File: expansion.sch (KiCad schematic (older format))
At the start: 4 parts, among them J10 Conn_02x05_Odd_Even, J7 DF40HC(3.5)-60DS, J9 DF40HC(3.5)-60DS, U1 IMX8MM

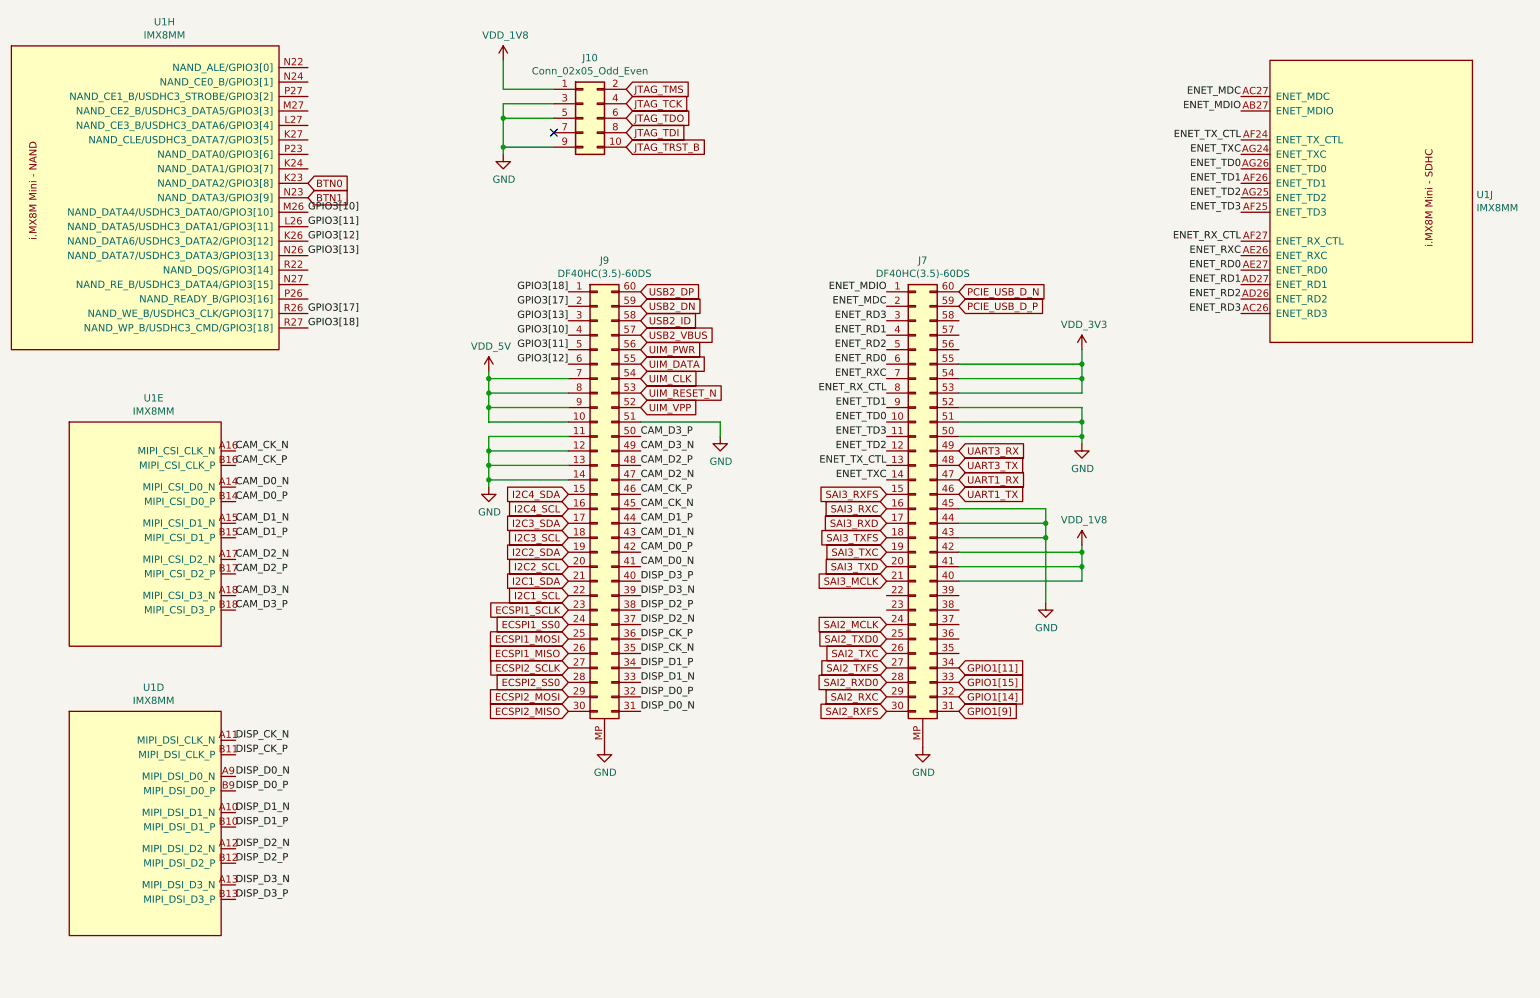
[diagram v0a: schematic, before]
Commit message: Change expansion audio routing to sai2/3
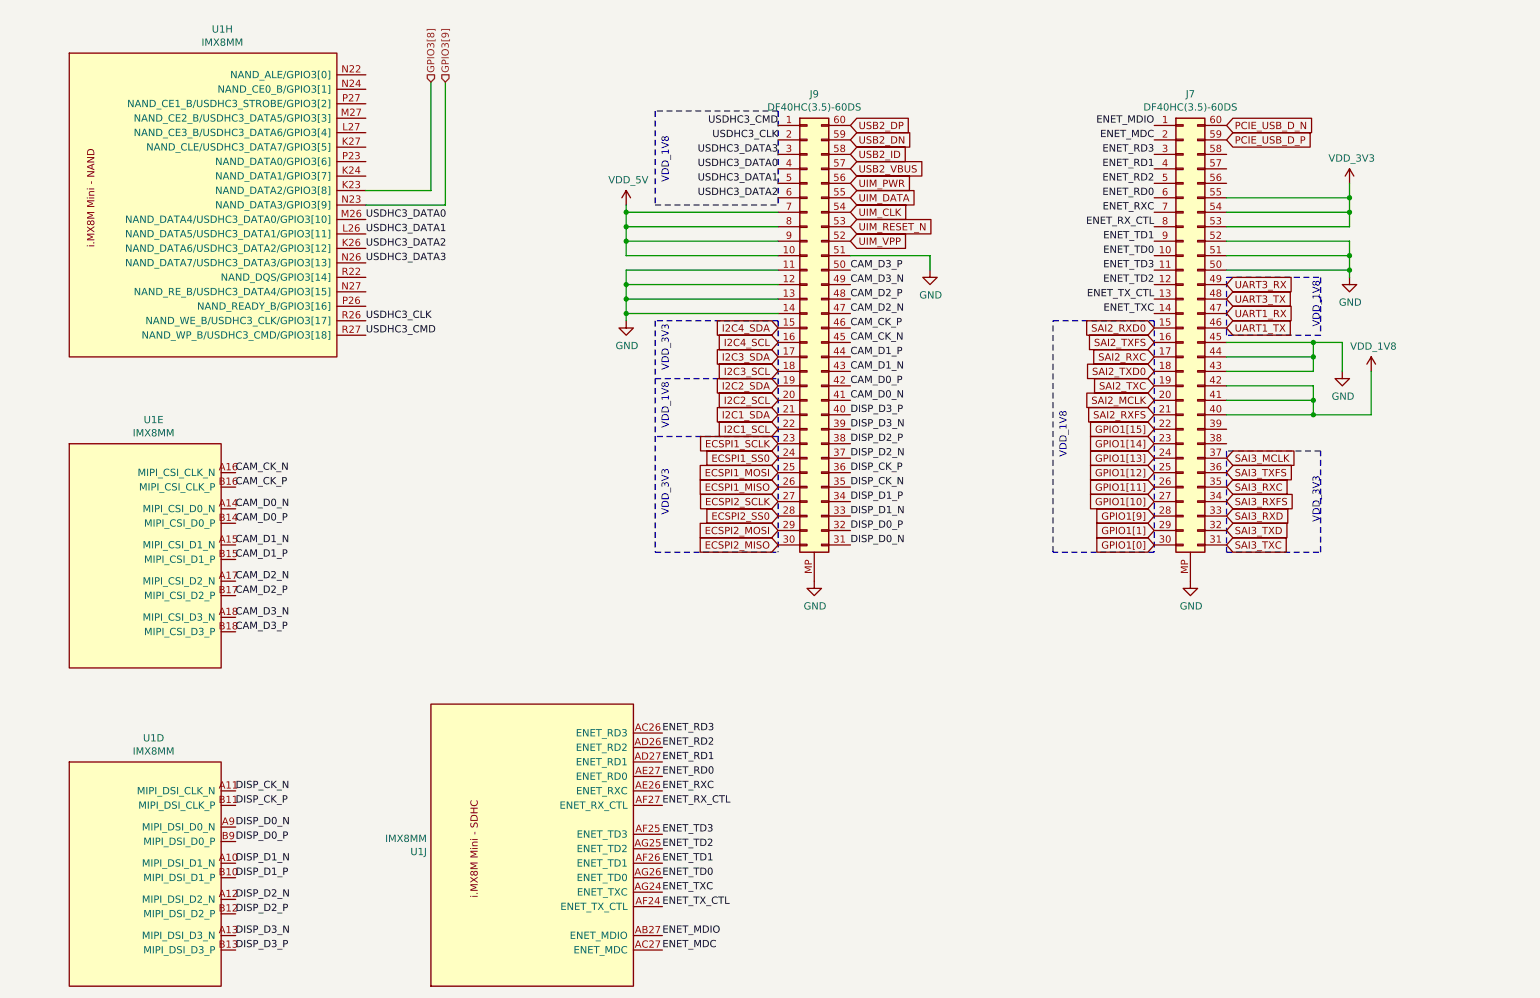
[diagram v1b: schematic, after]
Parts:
- removed J10: Conn_02x05_Odd_Even, Connector_PinHeader_1.27mm:PinHeader_2x05_P1.27mm_Vertical_SMD, symbol Connector_Generic:Conn_02x05_Odd_Even
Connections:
- net GPIO1[11]: now also J7.26 (Pin_26); no longer J7.34 (Pin_34)
- net GPIO1[14]: now also J7.23 (Pin_23); no longer J7.32 (Pin_32)
- net GPIO1[15]: now also J7.22 (Pin_22); no longer J7.33 (Pin_33)
- net GPIO1[9]: now also J7.28 (Pin_28); no longer J7.31 (Pin_31)
- net SAI2_MCLK: now also J7.20 (Pin_20); no longer J7.24 (Pin_24)
- net SAI2_RXC: now also J7.17 (Pin_17); no longer J7.29 (Pin_29)
- net SAI2_RXD0: now also J7.15 (Pin_15); no longer J7.28 (Pin_28)
- net SAI2_RXFS: now also J7.21 (Pin_21); no longer J7.30 (Pin_30)
- net SAI2_TXC: now also J7.19 (Pin_19); no longer J7.26 (Pin_26)
- net SAI2_TXD0: now also J7.18 (Pin_18); no longer J7.25 (Pin_25)
- net SAI2_TXFS: now also J7.16 (Pin_16); no longer J7.27 (Pin_27)
- net SAI3_MCLK: now also J7.37 (Pin_37); no longer J7.21 (Pin_21)
- net SAI3_RXC: now also J7.35 (Pin_35); no longer J7.16 (Pin_16)
- net SAI3_RXD: now also J7.33 (Pin_33); no longer J7.17 (Pin_17)
- net SAI3_RXFS: now also J7.34 (Pin_34); no longer J7.15 (Pin_15)
- net SAI3_TXC: now also J7.31 (Pin_31); no longer J7.19 (Pin_19)
- net SAI3_TXD: now also J7.32 (Pin_32); no longer J7.20 (Pin_20)
- net SAI3_TXFS: now also J7.36 (Pin_36); no longer J7.18 (Pin_18)
- net BTN0 renamed GPIO3[8]
- net BTN1 renamed GPIO3[9]
- net GPIO3[10] renamed USDHC3_DATA0
- net GPIO3[11] renamed USDHC3_DATA1
- net GPIO3[12] renamed USDHC3_DATA2
- net GPIO3[13] renamed USDHC3_DATA3
- net GPIO3[17] renamed USDHC3_CLK
- net GPIO3[18] renamed USDHC3_CMD
- new net GPIO1[0]: J7.30 (Pin_30)
- new net GPIO1[10]: J7.27 (Pin_27)
- new net GPIO1[12]: J7.25 (Pin_25)
- new net GPIO1[13]: J7.24 (Pin_24)
- new net GPIO1[1]: J7.29 (Pin_29)
- no-connect marks 1 -> 0
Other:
- note added: "VDD_1V8"
- note added: "VDD_3V3"
- moved on the sheet: J7, J9, U1D, U1E, U1H, U1J

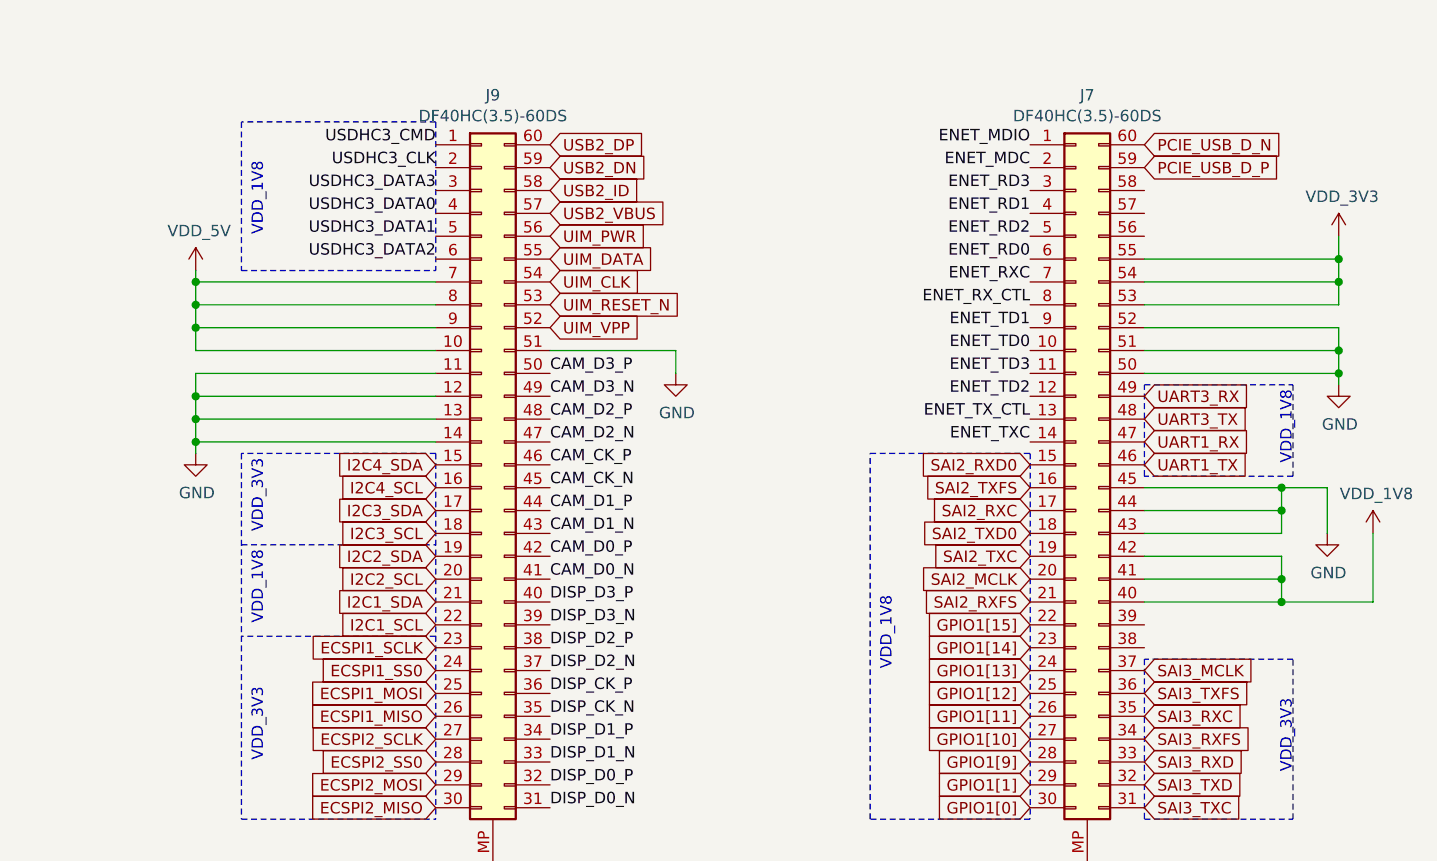
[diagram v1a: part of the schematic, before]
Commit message: Add esd protection to cc lines
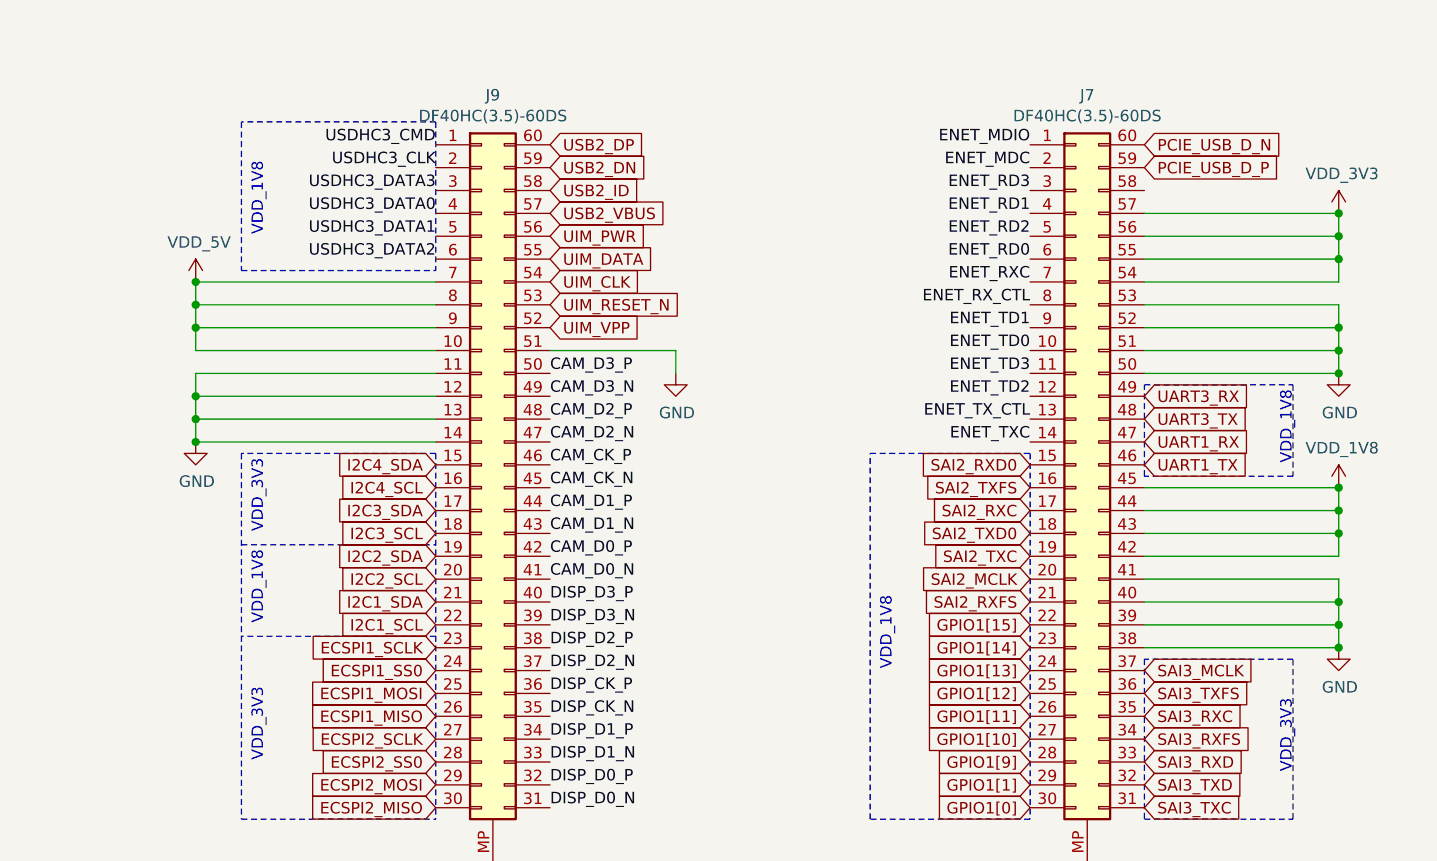
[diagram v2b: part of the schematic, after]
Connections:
- net GND: now also J7.38 (Pin_38), J7.39 (Pin_39), J7.40 (Pin_40), J7.41 (Pin_41), J7.53 (Pin_53); no longer J7.43 (Pin_43), J7.44 (Pin_44), J7.45 (Pin_45)
- net VDD_1V8: now also J7.43 (Pin_43), J7.44 (Pin_44), J7.45 (Pin_45); no longer J7.40 (Pin_40), J7.41 (Pin_41)
- net VDD_3V3: now also J7.56 (Pin_56), J7.57 (Pin_57); no longer J7.53 (Pin_53)
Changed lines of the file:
@@
 L mxenc:VDD_5V #PWR0220
 U 1 1 5F42799C
-P 4950 1950
-F 0 "#PWR0220" H 4950 1800 50  0001 C CNN
-F 1 "VDD_5V" H 4965 2123 50  0000 C CNN
-F 2 "" H 4950 1950 50  0001 C CNN
-F 3 "" H 4950 1950 50  0001 C CNN
-	1    4950 1950
-	1    0    0    -1
-$EndComp
-Wire Wire Line
-	4950 1950 4950 2000
+P 4950 2000
+F 0 "#PWR0220" H 4950 1850 50  0001 C CNN
+F 1 "VDD_5V" H 4965 2173 50  0000 C CNN
+F 2 "" H 4950 2000 50  0001 C CNN
+F 3 "" H 4950 2000 50  0001 C CNN
+	1    4950 2000
+	1    0    0    -1
+$EndComp
 Wire Wire Line
 	4950 2000 6000 2000
@@
 L power:GND #PWR0221
 U 1 1 5F42D118
-P 4950 2750
-F 0 "#PWR0221" H 4950 2500 50  0001 C CNN
-F 1 "GND" H 4955 2577 50  0000 C CNN
-F 2 "" H 4950 2750 50  0001 C CNN
-F 3 "" H 4950 2750 50  0001 C CNN
-	1    4950 2750
+P 4950 2700
+F 0 "#PWR0221" H 4950 2450 50  0001 C CNN
+F 1 "GND" H 4955 2527 50  0000 C CNN
+F 2 "" H 4950 2700 50  0001 C CNN
+F 3 "" H 4950 2700 50  0001 C CNN
+	1    4950 2700
 	1    0    0    -1
 $EndComp
 Wire Wire Line
 	6000 2700 4950 2700
-Wire Wire Line
-	4950 2700 4950 2750
 Wire Wire Line
 	6000 2600 4950 2600
@@
 L mxenc:VDD_1V8 #PWR0223
 U 1 1 5F46F757
-P 10100 3100
-F 0 "#PWR0223" H 10100 2950 50  0001 C CNN
-F 1 "VDD_1V8" H 10115 3273 50  0000 C CNN
-F 2 "" H 10100 3100 50  0001 C CNN
-F 3 "" H 10100 3100 50  0001 C CNN
-	1    10100 3100
-	1    0    0    -1
-$EndComp
-Wire Wire Line
-	9700 3400 9100 3400
-Wire Wire Line
-	9100 3300 9700 3300
-Connection ~ 9700 3300
-Wire Wire Line
-	9700 3300 9700 3400
-Wire Wire Line
-	9700 3200 9100 3200
-Wire Wire Line
-	9700 3200 9700 3300
+P 9950 2900
+F 0 "#PWR0223" H 9950 2750 50  0001 C CNN
+F 1 "VDD_1V8" H 9965 3073 50  0000 C CNN
+F 2 "" H 9950 2900 50  0001 C CNN
+F 3 "" H 9950 2900 50  0001 C CNN
+	1    9950 2900
+	1    0    0    -1
+$EndComp
+Wire Wire Line
+	9950 3100 9100 3100
+Wire Wire Line
+	9100 3000 9950 3000
+Connection ~ 9950 3000
+Wire Wire Line
+	9950 3000 9950 3100
+Wire Wire Line
+	9950 2900 9100 2900
+Wire Wire Line
+	9950 2900 9950 3000
 Text GLabel 9100 1400 2    50   Input ~ 0
 PCIE_USB_D_N
@@
 L power:GND #PWR0222
 U 1 1 5EFF4815
-P 9900 3100
-F 0 "#PWR0222" H 9900 2850 50  0001 C CNN
-F 1 "GND" H 9905 2927 50  0000 C CNN
-F 2 "" H 9900 3100 50  0001 C CNN
-F 3 "" H 9900 3100 50  0001 C CNN
-	1    9900 3100
-	1    0    0    -1
-$EndComp
-Wire Wire Line
-	9100 3100 9700 3100
-Wire Wire Line
-	9100 2900 9700 2900
-Wire Wire Line
-	9700 2900 9700 3000
-Wire Wire Line
-	9100 3000 9700 3000
-Connection ~ 9700 3000
-Wire Wire Line
-	9700 3000 9700 3100
+P 9950 3600
+F 0 "#PWR0222" H 9950 3350 50  0001 C CNN
+F 1 "GND" H 9955 3427 50  0000 C CNN
+F 2 "" H 9950 3600 50  0001 C CNN
+F 3 "" H 9950 3600 50  0001 C CNN
+	1    9950 3600
+	1    0    0    -1
+$EndComp
+Wire Wire Line
+	9100 3500 9950 3500
+Wire Wire Line
+	9100 3300 9950 3300
+Wire Wire Line
+	9950 3300 9950 3400
+Wire Wire Line
+	9100 3400 9950 3400
+Connection ~ 9950 3400
+Wire Wire Line
+	9950 3400 9950 3500
 $Comp
 L mxenc:VDD_3V3 #PWR0245
 U 1 1 5F185D48
-P 9950 1800
-F 0 "#PWR0245" H 9950 1650 50  0001 C CNN
-F 1 "VDD_3V3" H 9965 1973 50  0000 C CNN
-F 2 "" H 9950 1800 50  0001 C CNN
-F 3 "" H 9950 1800 50  0001 C CNN
-	1    9950 1800
-	1    0    0    -1
-$EndComp
-Wire Wire Line
-	9950 1800 9950 1900
-Wire Wire Line
-	9950 1900 9100 1900
-Wire Wire Line
-	9950 1900 9950 2000
-Wire Wire Line
-	9950 2000 9100 2000
-Connection ~ 9950 1900
-Wire Wire Line
-	9100 2100 9950 2100
-Wire Wire Line
-	9950 2100 9950 2000
-Connection ~ 9950 2000
+P 9950 1700
+F 0 "#PWR0245" H 9950 1550 50  0001 C CNN
+F 1 "VDD_3V3" H 9965 1873 50  0000 C CNN
+F 2 "" H 9950 1700 50  0001 C CNN
+F 3 "" H 9950 1700 50  0001 C CNN
+	1    9950 1700
+	1    0    0    -1
+$EndComp
+Wire Wire Line
+	9950 1700 9100 1700
+Wire Wire Line
+	9950 1700 9950 1800
+Wire Wire Line
+	9950 1800 9100 1800
+Connection ~ 9950 1700
+Wire Wire Line
+	9100 1900 9950 1900
+Wire Wire Line
+	9950 1900 9950 1800
+Connection ~ 9950 1800
 $Comp
 L power:GND #PWR0253
 U 1 1 5F18CEE2
-P 9950 2450
-F 0 "#PWR0253" H 9950 2200 50  0001 C CNN
-F 1 "GND" H 9955 2277 50  0000 C CNN
-F 2 "" H 9950 2450 50  0001 C CNN
-F 3 "" H 9950 2450 50  0001 C CNN
-	1    9950 2450
-	1    0    0    -1
-$EndComp
-Wire Wire Line
-	9950 2450 9950 2400
+P 9950 2400
+F 0 "#PWR0253" H 9950 2150 50  0001 C CNN
+F 1 "GND" H 9955 2227 50  0000 C CNN
+F 2 "" H 9950 2400 50  0001 C CNN
+F 3 "" H 9950 2400 50  0001 C CNN
+	1    9950 2400
+	1    0    0    -1
+$EndComp
 Wire Wire Line
 	9950 2200 9100 2200
@@
 VDD_1V8
 Wire Wire Line
-	10100 3400 9700 3400
-Connection ~ 9700 3400
-Wire Wire Line
-	9700 2900 9900 2900
-Wire Wire Line
-	9900 2900 9900 3100
-Connection ~ 9700 2900
-Wire Wire Line
-	10100 3100 10100 3400
+	9950 3100 9950 3200
 Text Label 3150 2050 0    50   ~ 0
 USDHC3_DATA0
 Text Label 3150 2250 0    50   ~ 0
 USDHC3_DATA2
+Wire Wire Line
+	9100 3200 9950 3200
+Connection ~ 9950 3100
+Wire Wire Line
+	9100 3600 9950 3600
+Wire Wire Line
+	9950 3600 9950 3500
+Connection ~ 9950 3500
+Connection ~ 9950 3600
+Connection ~ 9950 2900
+Wire Wire Line
+	9100 2100 9950 2100
+Wire Wire Line
+	9950 2100 9950 2200
+Connection ~ 9950 2200
+Wire Wire Line
+	9100 2000 9950 2000
+Wire Wire Line
+	9950 2000 9950 1900
+Connection ~ 9950 1900
 $EndSCHEMATC

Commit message: Set up for battery NTC and add a power button
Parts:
- J7, J9: symbol Connector_Generic:Conn_02x30_Counter_Clockwise -> Connector_Generic_MountingPin:Conn_02x30_Counter_Clockwise_MountingPin; Mfgr (none) -> Hirose; Part (none) -> DF40C-60DP-0.4V(51); Vendorpart (none) -> H11628CT-ND
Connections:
- net VDD_5V renamed VSYS_5V
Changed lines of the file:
@@
 EESchema Schematic File Version 4
-LIBS:mxenc-cache
-EELAYER 29 0
+EELAYER 30 0
 EELAYER END
 $Descr A4 11693 8268
 encoding utf-8
 Sheet 9 10
-Title ""
-Date ""
-Rev ""
-Comp ""
+Title "kimχ micro"
+Date "2020-03-05"
+Rev "0.9"
+Comp "GroupGets"
 Comment1 ""
 Comment2 ""
@@
 $EndDescr
 $Comp
-L Connector_Generic:Conn_02x30_Counter_Clockwise J?
+L Connector_Generic_MountingPin:Conn_02x30_Counter_Clockwise_MountingPin J?
 U 1 1 5E367446
 P 6200 2800
@@
 F 2 "mxenc:DF40C-60DP" H 6200 2800 50  0001 C CNN
 F 3 "~" H 6200 2800 50  0001 C CNN
+F 4 "H11628CT-ND" H 6200 2800 50  0000 C CNN "Vendorpart"
+F 5 "Hirose" H 6200 2800 50  0001 C CNN "Mfgr"
+F 6 "DF40C-60DP-0.4V(51)" H 6200 2800 50  0001 C CNN "Part"
 	1    6200 2800
 	1    0    0    -1
 $EndComp
 $Comp
-L Connector_Generic:Conn_02x30_Counter_Clockwise J?
+L Connector_Generic_MountingPin:Conn_02x30_Counter_Clockwise_MountingPin J?
 U 1 1 5E36744C
 P 8800 2800
@@
 F 2 "mxenc:DF40C-60DP" H 8800 2800 50  0001 C CNN
 F 3 "~" H 8800 2800 50  0001 C CNN
+F 4 "H11628CT-ND" H 8800 2800 50  0000 C CNN "Vendorpart"
+F 5 "Hirose" H 8800 2800 50  0001 C CNN "Mfgr"
+F 6 "DF40C-60DP-0.4V(51)" H 8800 2800 50  0001 C CNN "Part"
 	1    8800 2800
 	1    0    0    -1
@@
 Wire Wire Line
 	7050 2300 6500 2300
-$Comp
-L mxenc:VDD_5V #PWR0220
-U 1 1 5F42799C
-P 4950 2000
-F 0 "#PWR0220" H 4950 1850 50  0001 C CNN
-F 1 "VDD_5V" H 4965 2173 50  0000 C CNN
-F 2 "" H 4950 2000 50  0001 C CNN
-F 3 "" H 4950 2000 50  0001 C CNN
-	1    4950 2000
-	1    0    0    -1
-$EndComp
 Wire Wire Line
 	4950 2000 6000 2000
@@
 Wire Wire Line
 	4950 2300 4950 2200
-Connection ~ 4950 2000
 Wire Wire Line
 	6000 2200 4950 2200
@@
 	4950 2500 4950 2600
 Connection ~ 4950 2600
-Wire Wire Line
-	6000 2400 4950 2400
-Wire Wire Line
-	4950 2400 4950 2500
-Connection ~ 4950 2500
 $Comp
 L mxenc:VDD_1V8 #PWR0223
@@
 	9950 2000 9950 1900
 Connection ~ 9950 1900
+$Comp
+L mxenc:VSYS_5V #PWR0220
+U 1 1 5E69C086
+P 4950 1900
+F 0 "#PWR0220" H 4950 1750 50  0001 C CNN
+F 1 "VSYS_5V" H 4965 2073 50  0000 C CNN
+F 2 "" H 4950 1900 50  0001 C CNN
+F 3 "" H 4950 1900 50  0001 C CNN
+	1    4950 1900
+	1    0    0    -1
+$EndComp
+Wire Wire Line
+	4950 1900 4950 2000
+Connection ~ 4950 2000
+Connection ~ 4950 2500
+Wire Wire Line
+	4950 2400 4950 2500
+Wire Wire Line
+	6000 2400 4950 2400
+Wire Wire Line
+	6250 4500 6250 4550
+Wire Wire Line
+	8850 4500 8850 4550
 $EndSCHEMATC
